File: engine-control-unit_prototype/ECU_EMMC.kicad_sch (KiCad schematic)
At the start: 17 parts, among them IC1 ASFC32G31T3-51BIN

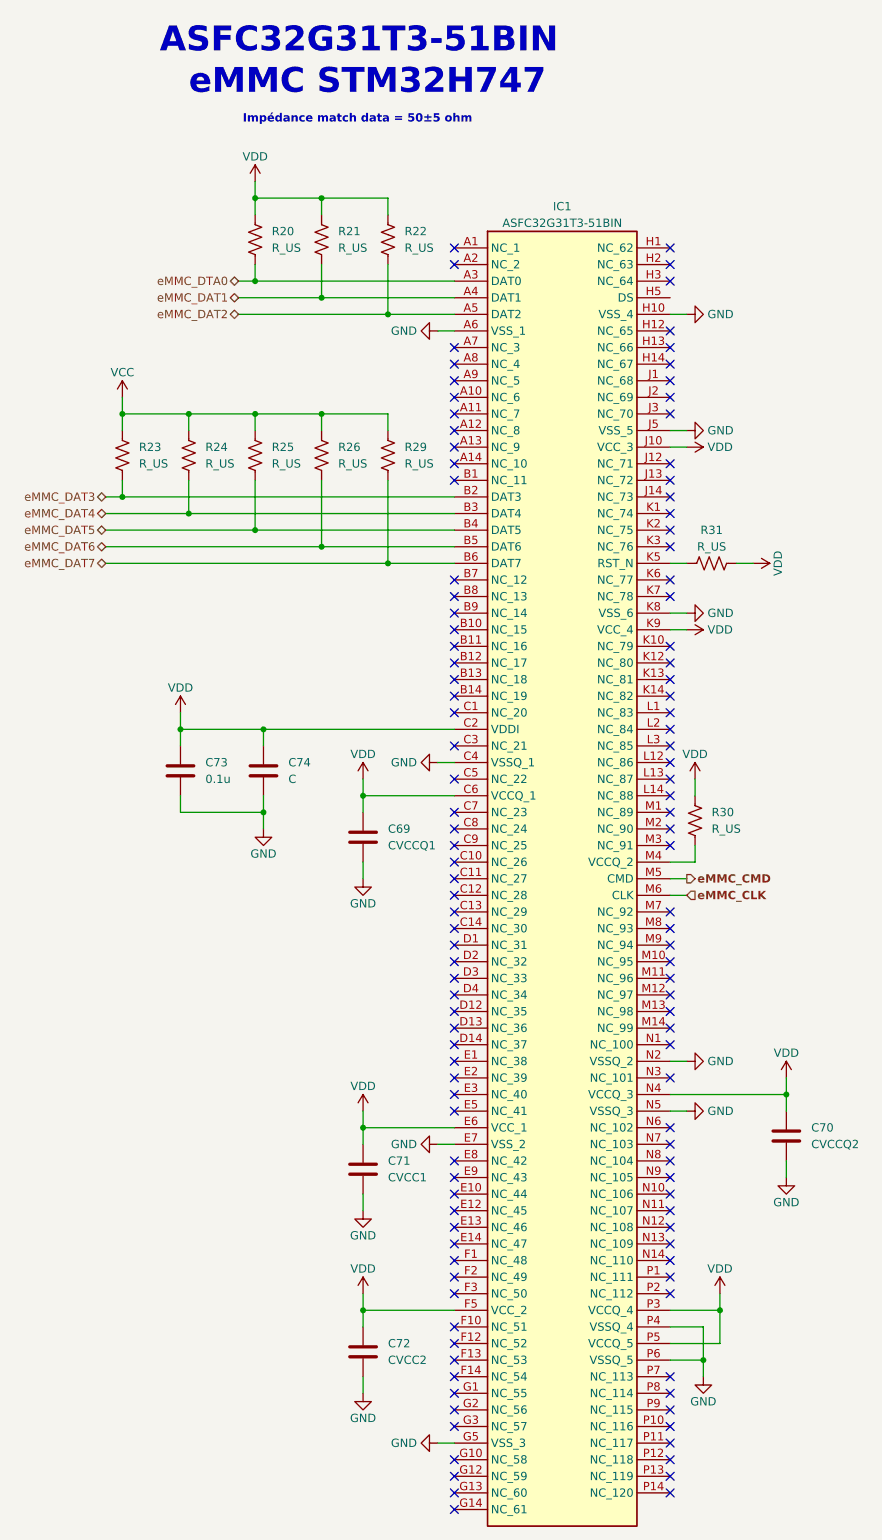
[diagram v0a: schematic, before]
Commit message: Added power circuitry without components values
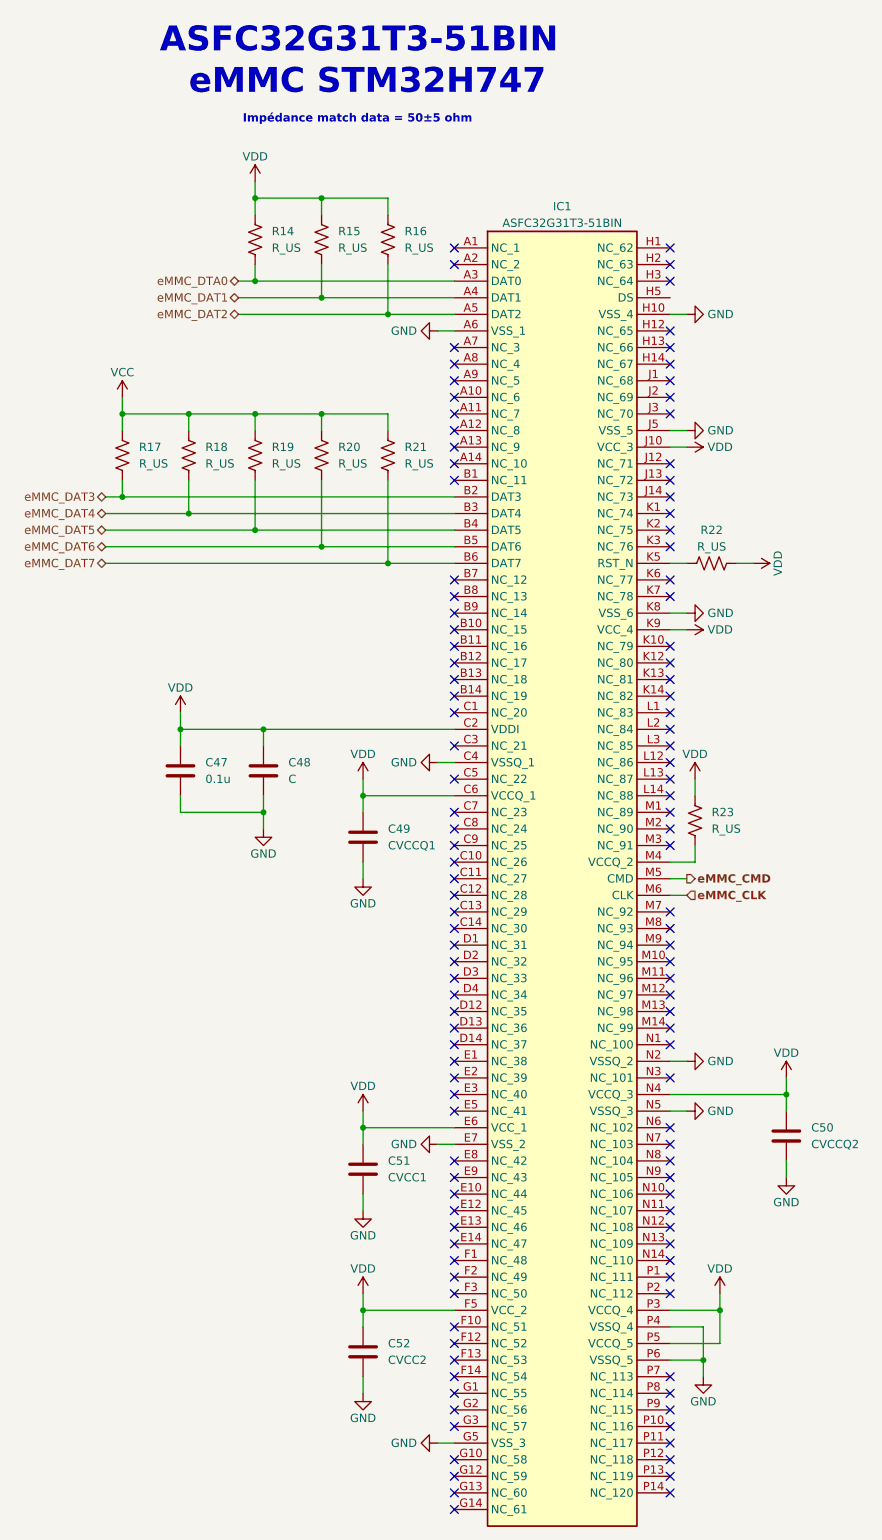
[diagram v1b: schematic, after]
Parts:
- renumbered C73 to C47, C74 to C48, C69 to C49, C70 to C50, C71 to C51, C72 to C52, R20 to R14, R21 to R15, R22 to R16, R23 to R17, R24 to R18, R25 to R19, R26 to R20, R29 to R21, R31 to R22, R30 to R23

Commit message: Removed bloat libraries Changed symbols for Sirius custom library Changed layout for one page
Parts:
- removed C47: 0.1u, symbol Device:C
- removed C48: C, symbol Device:C
- removed C49: CVCCQ1, symbol Device:C
- removed C50: CVCCQ2, symbol Device:C
- removed C51: CVCC1, symbol Device:C
- removed C52: CVCC2, symbol Device:C
- removed IC1: ASFC32G31T3-51BIN, BGA153C50P14X14_1300X1150X120, symbol ASFC32G31T3-51BIN:ASFC32G31T3-51BIN
- removed R14, R15, R16, R17, R18, R19, R20, R21, R22, R23: R_US, symbol Device:R_US
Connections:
- no-connect marks 120 -> 0
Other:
- note removed: "ASFC32G31T3-51BIN"
- note removed: "Impédance match data = 50±5 ohm"
- note removed: "eMMC STM32H747"
